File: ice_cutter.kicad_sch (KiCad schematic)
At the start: 54 parts

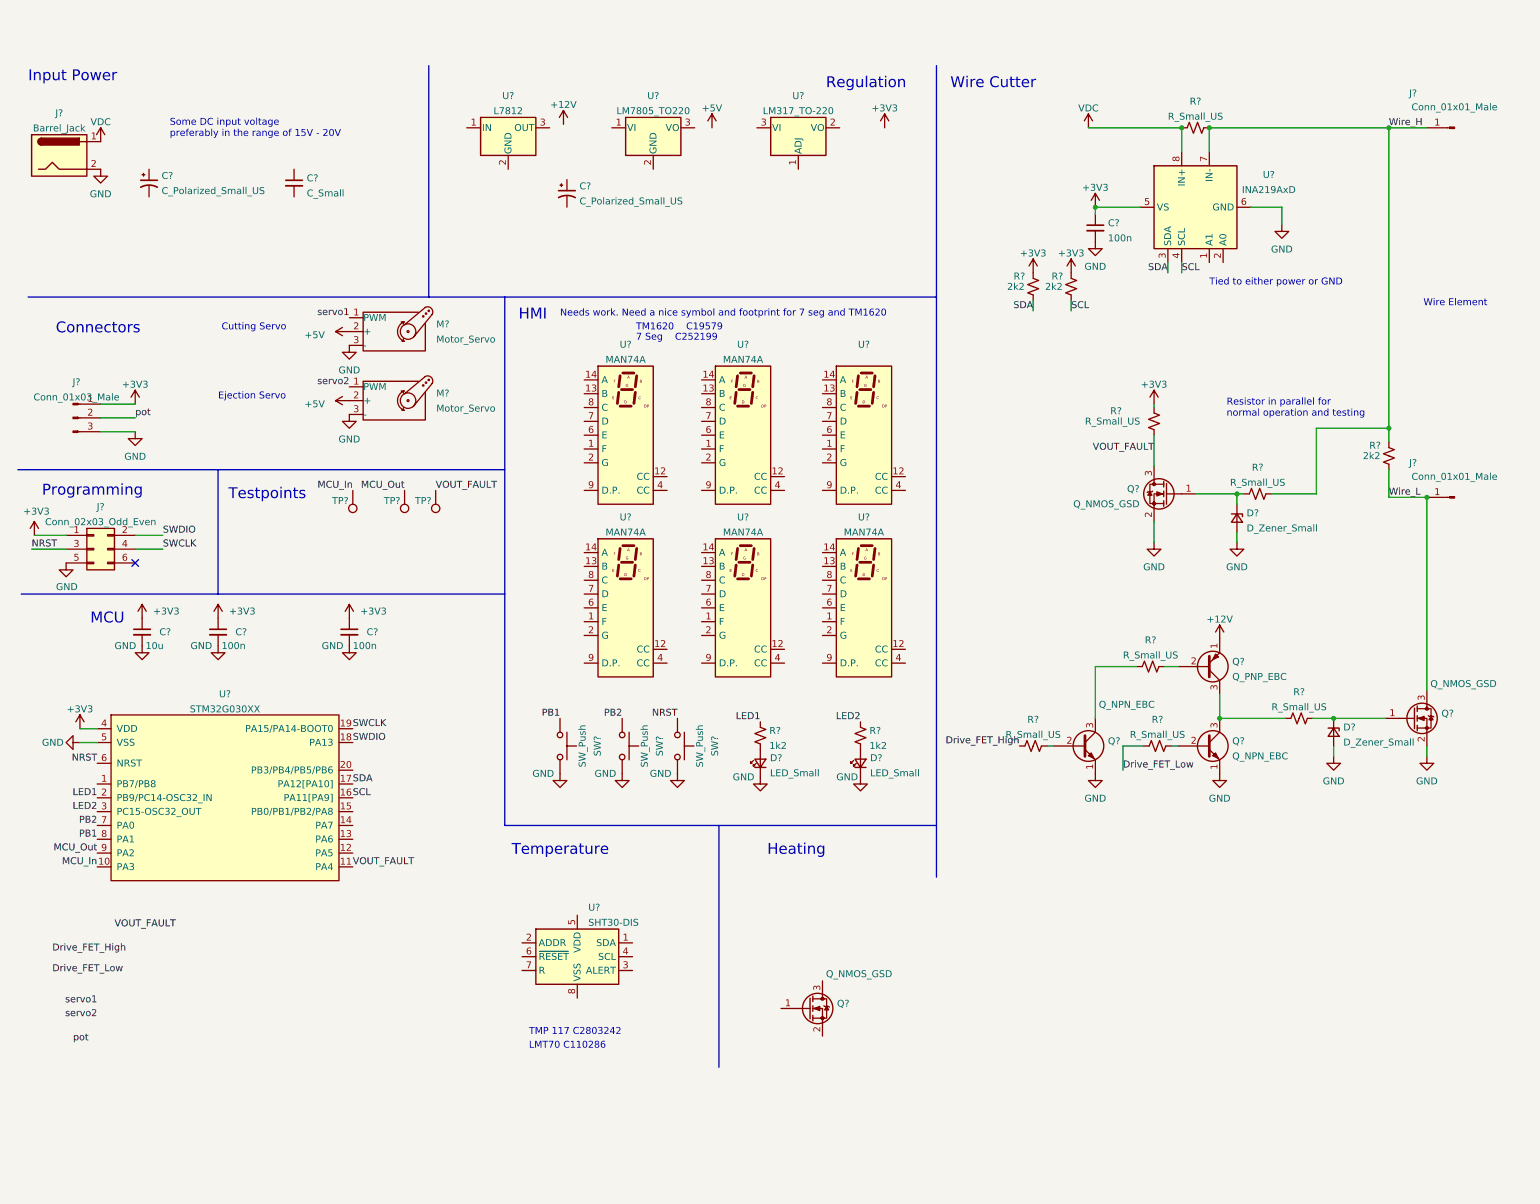
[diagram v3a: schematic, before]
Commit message: Changes in schematic, added Soft starts everywhere...
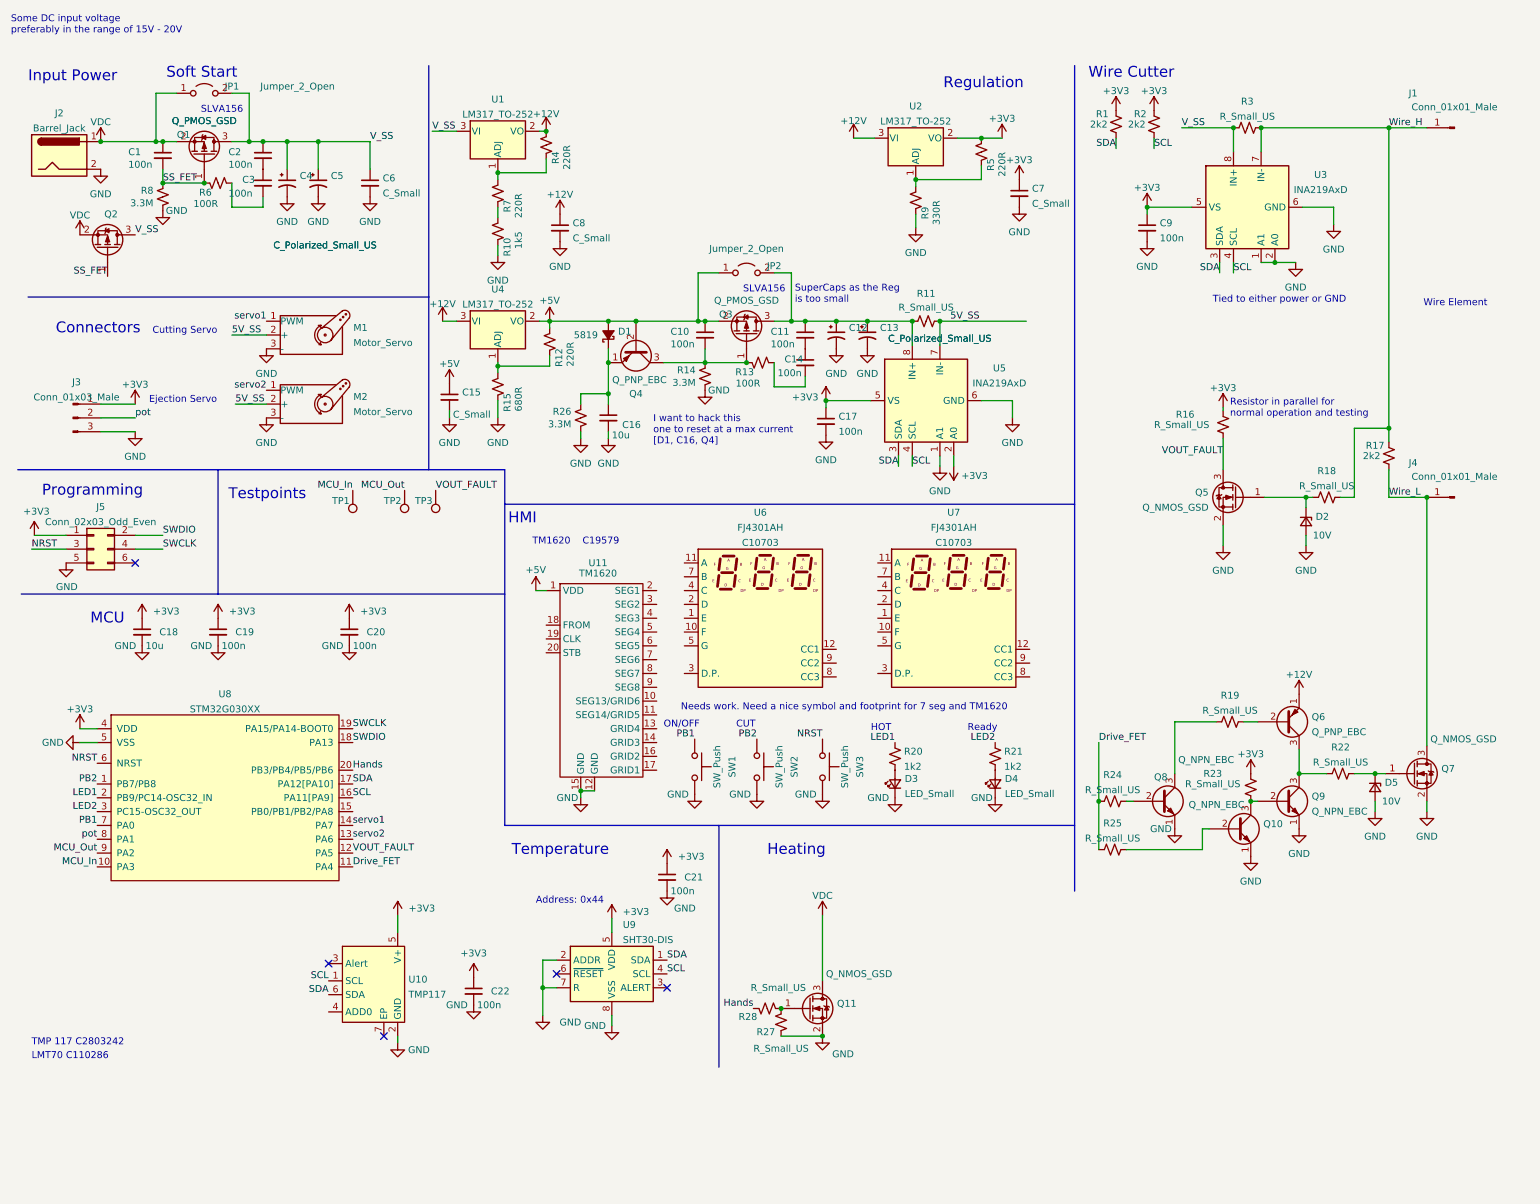
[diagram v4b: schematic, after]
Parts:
- removed C?: C_Polarized_Small_US, symbol Device:C_Polarized_Small_US
- removed D? (x2): LED_Small, symbol Device:LED_Small
- removed D?: D_Zener_Small, symbol Device:D_Zener_Small
- removed R? (x2): 1k2, symbol Device:R_Small_US
- removed SW? (x3): SW_Push, symbol Switch:SW_Push
- removed U? (x5): MAN74A, Display_7Segment:MAN71A, symbol Display_Character:MAN74A
- removed U?: (no value), symbol Display_Character:MAN74A
- removed U?: LM317_TO-220, Package_TO_SOT_THT:TO-220-3_Vertical, symbol Regulator_Linear:LM317_TO-220
- removed U?: LM7805_TO220, Package_TO_SOT_THT:TO-220-3_Vertical, symbol Regulator_Linear:LM7805_TO220
- removed U?: L7812, symbol Regulator_Linear:L7812
- added C1, C10, C11, C14, C2, C21, C22, C3: 100n, Capacitor_SMD:C_0402_1005Metric, symbol Device:C_Small
- added C12, C13, C4: C_Polarized_Small_US, symbol Device:C_Polarized_Small_US
- added C15, C7, C8: C_Small, symbol Device:C_Small
- added C16: 10u, symbol Device:C_Small
- added C17: 100n, symbol Device:C_Small
- added D1: 5819, Diode_SMD:D_SOD-123, symbol Device:D_Schottky_Small_Filled
- added D2: 10V, Diode_SMD:D_SOD-123, symbol Device:D_Zener_Small
- added D3, D4: LED_Small, Diode_SMD:D_0603_1608Metric, symbol Device:LED_Small
- added JP1, JP2: Jumper_2_Open, Jumper:SolderJumper-2_P1.3mm_Open_RoundedPad1.0x1.5mm, symbol Jumper:Jumper_2_Open
- added Q1, Q2, Q3: Q_PMOS_GSD, Package_TO_SOT_SMD:SOT-23, symbol Device:Q_PMOS_GSD
- added Q10: Q_NPN_EBC, symbol Device:Q_NPN_EBC
- added Q4: Q_PNP_EBC, symbol Device:Q_PNP_EBC
- added R10: 1k5, Resistor_SMD:R_0402_1005Metric, symbol Device:R_Small_US
- added R11, R25, R27, R28: R_Small_US, Resistor_SMD:R_0402_1005Metric, symbol Device:R_Small_US
- added R12, R4, R5, R7: 220R, Resistor_SMD:R_0402_1005Metric, symbol Device:R_Small_US
- added R13, R6: 100R, Resistor_SMD:R_0402_1005Metric, symbol Device:R_Small_US
- added R14, R26, R8: 3.3M, Resistor_SMD:R_0402_1005Metric, symbol Device:R_Small_US
- added R15: 680R, Resistor_SMD:R_0402_1005Metric, symbol Device:R_Small_US
- added R20, R21: 1k2, Resistor_SMD:R_0402_1005Metric, symbol Device:R_Small_US
- added R9: 330R, Resistor_SMD:R_0402_1005Metric, symbol Device:R_Small_US
- added SW1, SW2, SW3: SW_Push, Button_Switch_SMD:SW_SPST_TL3342, symbol Switch:SW_Push
- added U1, U2, U4: LM317_TO-252, Package_TO_SOT_SMD:TO-252-2, symbol Regulator_Linear:LM317_TO-252
- added U10: TMP117, symbol UCT:TMP117
- added U11: TM1620, Package_SO:SOP-20_7.5x12.8mm_P1.27mm, symbol LED_drive_control:TM1620
- added U5: INA219AxD, Package_SO:SOIC-8_3.9x4.9mm_P1.27mm, symbol Analog_ADC:INA219AxD
- added U6, U7: FJ4301AH, UCT:7_Seg_x3, symbol UCT:FJ4301AH
- C5, C6, C9: renamed from C?; Populate (none) -> Yes
- D5: renamed from D?; value D_Zener_Small -> 10V; footprint (none) -> Diode_SMD:D_SOD-123; Extended (none) -> 1; LCSC (none) -> C173429; Populate (none) -> Yes; Price (none) -> 0.02
- J1, J4: renamed from J?; footprint (none) -> Connector_PinHeader_2.54mm:PinHeader_1x01_P2.54mm_Vertical; Populate (none) -> No
- J2: renamed from J?; Extended (none) -> 1; LCSC (none) -> C84007; Populate (none) -> Yes
- J3: renamed from J?; footprint (none) -> Connector_PinHeader_2.54mm:PinHeader_1x03_P2.54mm_Vertical; Populate (none) -> No
- M1, M2: renamed from M?; footprint (none) -> Connector_PinHeader_2.54mm:PinHeader_1x03_P2.54mm_Vertical; Populate (none) -> No
- Q11, Q5, Q6, Q8, Q9: renamed from Q?; Populate (none) -> Yes
- Q7: renamed from Q?; footprint (none) -> Package_TO_SOT_SMD:TO-252-2; Extended (none) -> 1; LCSC (none) -> C130980; Populate (none) -> Yes; Price (none) -> 0.2
- R1, R16, R17, R18, R19, R2, R22, R23, R24, R3: renamed from R?; footprint (none) -> Resistor_SMD:R_0402_1005Metric; Populate (none) -> Yes
- U3, U9: renamed from U?; Populate (none) -> Yes
- gave numbers to parts that had none: 8
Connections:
- net Drive_FET_Low is gone; now on an unnamed net: R23.1
- net +12V: now also C8.1, R4.2, U1.2 (VO), U2.3 (VI), U4.3 (VI)
- net +3V3: now also R23.2, U9.5 (VDD), C17.1, C21.1, C22.1, C7.1, R5.2, U10.5 (V+), U2.2 (VO), U5.2 (A0), U5.5 (VS)
- net +5V: now also C10.1, C15.1, D1.2 (A), JP2.1 (A), Q3.2 (S), Q4.2 (B), R12.2, U11.1 (VDD), U4.2 (VO); no longer M1.2 (+), M2.2 (+)
- net GND: now also C5.2, C6.2, Q11.2 (S), U3.1 (A1), U3.2 (A0), U9.2 (ADDR), U9.7 (R), U9.8 (VSS), U9.9 (VSS), C12.2, C13.2, C15.2, C16.2, C17.2, C21.2, C22.2, C4.2, C7.2, C8.2, D2.2 (A), D3.1 (K), D4.1 (K), Q10.1 (E), R10.1, R14.2, R15.1, R26.2, R28.2, R8.2, R9.1, SW1.2, SW2.2, SW3.2, U10.2 (GND), U11.12 (GND), U11.15 (GND), U5.1 (A1), U5.6 (GND)
- net LED1: now also R20.1
- net LED2: now also R21.1
- net NRST: now also SW3.1
- net PB1: now also U8.7 (PA0), SW1.1; no longer U8.8 (PA1)
- net PB2: now also U8.1 (PB7/PB8), SW2.1; no longer U8.7 (PA0)
- net SCL: now also U9.4 (SCL), U10.1 (SCL), U5.4 (SCL)
- net SDA: now also U9.1 (SDA), U10.6 (SDA), U5.3 (SDA)
- net VDC: now also Q11.3 (D), C1.1, JP1.1 (A), Q1.2 (S), Q2.2 (S); no longer R3.1, U3.8 (IN+)
- net VOUT_FAULT: now also U8.12 (PA5); no longer U8.11 (PA4)
- net pot: now also U8.8 (PA1)
- net servo1: now also U8.14 (PA7)
- net servo2: now also U8.13 (PA6)
- net V_SS: now reaches C5.1
- net V_SS: now also C6.1, R3.1, U3.8 (IN+), C2.1, C4.1, JP1.2 (B), Q1.3 (D), Q2.3 (D), U1.3 (VI)
- net at Q5.1 (G), R18.1: now also D2.1 (K)
- net at Q9.2 (B): now also Q10.3 (C); no longer R23.2
- net at Q11.1 (G): now also R27.2, R28.1
- net Hands: now reaches U8.20 (PB3/PB4/PB5/PB6)
- net Hands: now also R27.1
- net Drive_FET_High renamed Drive_FET
- net Drive_FET: now also U8.11 (PA4), R25.1
- new net: C11.1, C12.1, C13.1, JP2.2 (B), Q3.3 (D), R11.1, U5.8 (IN+)
- new net: C11.2, C14.1
- new net: C10.2, Q3.1 (G), Q4.3 (C), R13.1, R14.1
- new net: R5.1, R9.2, U2.1 (ADJ)
- new net: C2.2, C3.1
- new net: D3.2 (A), R20.2
- new net: Q10.2 (B), R25.2
- new net: R4.1, R7.2, U1.1 (ADJ)
- new net: D4.2 (A), R21.2
- new net: C16.1, D1.1 (K), Q4.1 (E), R26.1
- new net: C3.2, R6.2
- new net: R12.1, R15.2, U4.1 (ADJ)
- new net: C14.2, R13.2
- new net: R10.2, R7.1
- new net 5V_SS: M1.2 (+), M2.2 (+), R11.2, U5.7 (IN-)
- new net SS_FET: C1.2, Q1.1 (G), Q2.1 (G), R6.1, R8.1
- no-connect marks 1 -> 5
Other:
- note added: "Address: 0x44"
- note added: "CUT"
- note added: "HOT"
- note added: "I want to hack this one to reset at a max current [D1, C16, Q4]"
- note added: "ON/OFF"
- note added: "Ready"
- note added: "SLVA156"
- note added: "Soft Start"
- note added: "SuperCaps as the Reg is too small"
- note removed: "7 Seg C252199"
- moved on the sheet: C5, C6, C9, D5, M1, M2, Q5, Q6, Q7, Q8, Q9, R1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
